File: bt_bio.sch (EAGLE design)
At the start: 75 parts, among them U1 ADP121-AUJZ33R7, U2 MCP73837-FCI/UN, U4 ADP121-AUJZ18R7, U5 LSM9DS1, X1 53047-03, X2 MINI-USB-SHIELD-UX60-MB-5ST, X3 53047-03

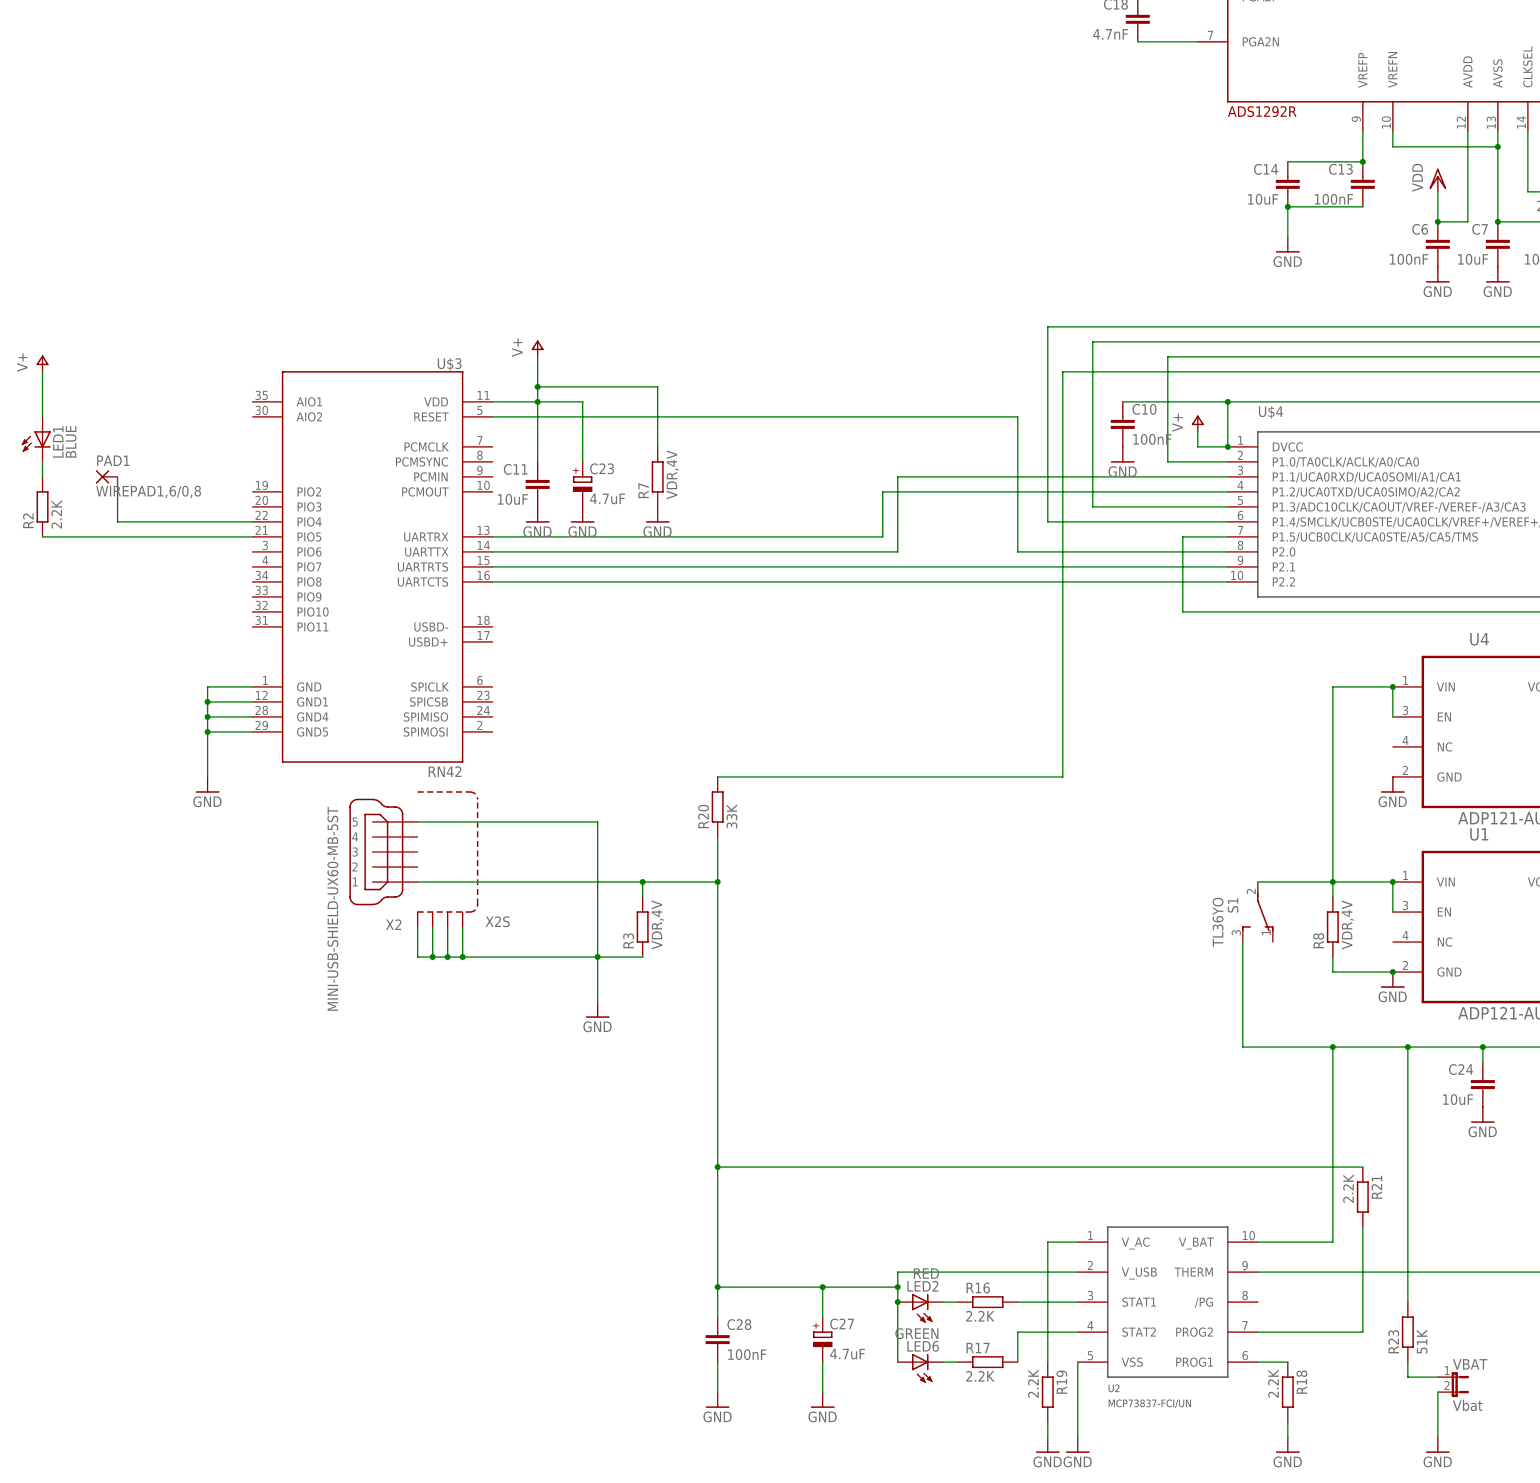
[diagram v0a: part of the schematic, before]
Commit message: switched to RN4678
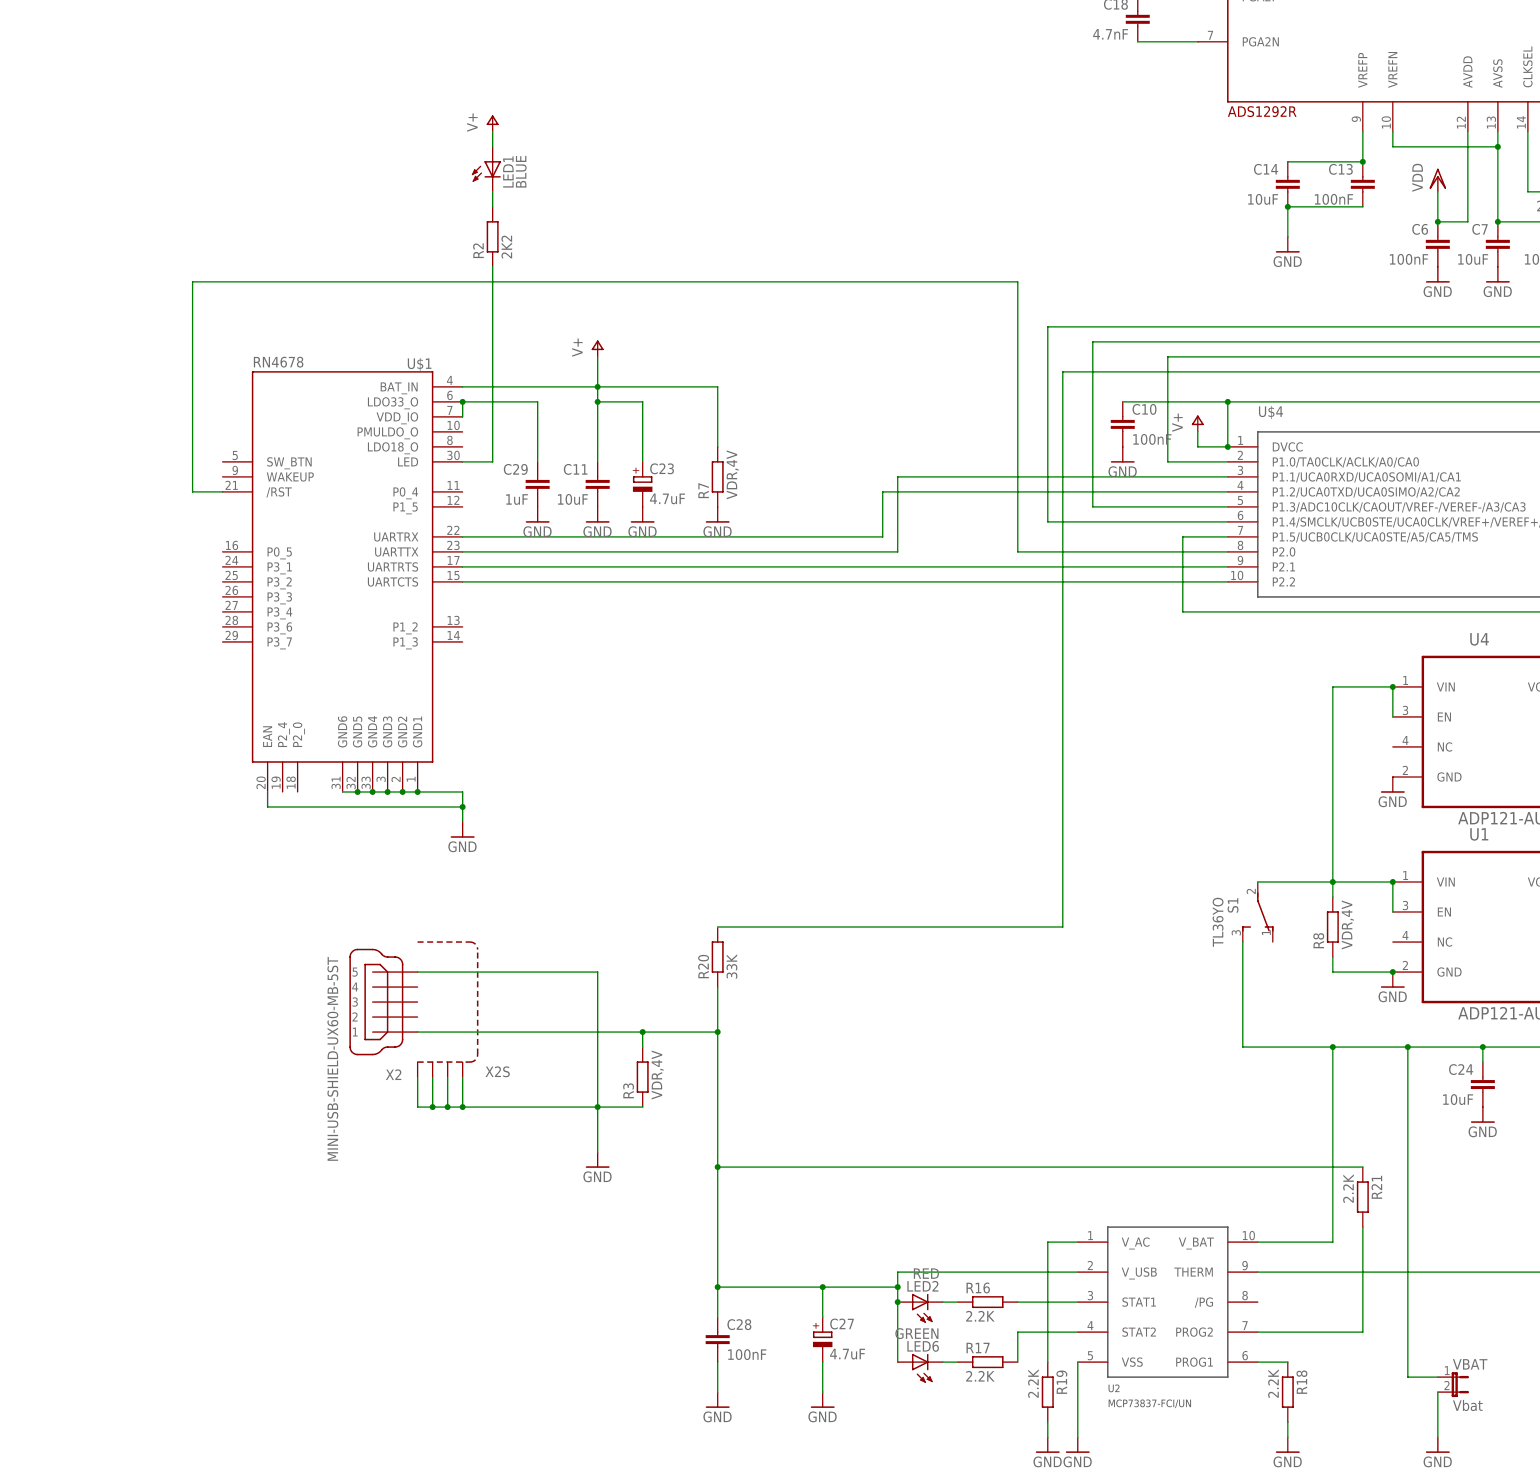
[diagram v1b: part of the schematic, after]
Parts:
- removed PAD1: WIREPAD1,6/0,8, wirepad:WIREPAD1,6/0,8
- removed R23: 51K, rcl:R-EU_R0603
- removed U$3: RN42, RN42__BoB:SPARKFUN_BLUETOOTH-RN41"
- added C29: 1uF, rcl:C-EUC1206
- added U$1: RN4678, rn4678:RN4678
- R2: value 2.2K -> 2K2
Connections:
- removed net N$10: R2.1, U$3.PIO5
- removed net N$14: PAD1.P, U$3.PIO4
- removed net N$46: C24.1, R23.2, S1.S, U2.V_BAT, X3-1.S
- removed net N$7: U$3.UARTRTS, U$4.P2.1
- removed net N$8: U$3.UARTCTS, U$4.P2.2
- removed net N$9: U$3.RESET, U$4.P2.0
- new net CTS: U$1.UARTCTS, U$4.P2.2
- new net RESET: U$1./RST, U$4.P2.0
- new net RTS: U$1.UARTRTS, U$4.P2.1
- new net RX: U$1.UARTRX, U$4.P1.2/UCA0TXD/UCA0SIMO/A2/CA2
- new net TX: U$1.UARTTX, U$4.P1.1/UCA0RXD/UCA0SOMI/A1/CA1
- net GND: now also C29.2, U$1.EAN, U$1.GND1, U$1.GND2, U$1.GND3, U$1.GND4, U$1.GND5, U$1.GND6; no longer U$3.GND, U$3.GND1, U$3.GND4, U$3.GND5
- net N$2: now also C29.1, U$1.LDO33_O, U$1.VDD_IO; no longer U$3.UARTRX, U$4.P1.2/UCA0TXD/UCA0SIMO/A2/CA2
- net N$31: now also C24.1, S1.S, U2.V_BAT, X3-1.S; no longer R23.1
- net N$6: now also R2.1, U$1.LED; no longer U$3.UARTTX, U$4.P1.1/UCA0RXD/UCA0SOMI/A1/CA1
- net V+: now also U$1.BAT_IN; no longer U$3.VDD
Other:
- moved on the sheet: C11, C23, LED1, R2, R20, R3, R7, X2, X2S

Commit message: Version European Circiuts
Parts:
- C29: device rcl:C-EUC1206 -> rcl:C-EUC0603
- R2: value 2K2 -> 2.2K
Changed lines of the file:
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@@
 <part name="P+3" library="supply1" deviceset="V+" device=""/>
 <part name="LED1" library="led" deviceset="LED" device="CHIPLED_0805" value="BLUE"/>
-<part name="R2" library="rcl" deviceset="R-EU_" device="R0603" value="2K2"/>
+<part name="R2" library="rcl" deviceset="R-EU_" device="R0603" value="2.2K"/>
 <part name="P+4" library="supply1" deviceset="V+" device=""/>
 <part name="C10" library="rcl" deviceset="C-EU" device="C0603" value="100nF"/>
@@
 <part name="C24" library="rcl" deviceset="C-EU" device="C1206" value="10uF"/>
 <part name="U$1" library="rn4678" deviceset="RN4678" device=""/>
-<part name="C29" library="rcl" deviceset="C-EU" device="C1206" value="1uF"/>
+<part name="C29" library="rcl" deviceset="C-EU" device="C0603" value="1uF"/>
 <part name="GND16" library="supply1" deviceset="GND" device=""/>
 </parts>
